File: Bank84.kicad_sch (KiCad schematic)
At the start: 1 part, among them U1 XCKU5P-FFVB676

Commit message: finishing schematic
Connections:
- net IO_L11N_AD1N_84_N: now reaches U1.AA13 (IO_L11N_AD1N_84_N)
- net IO_L8P_HDGC_AD4P_84_P: now reaches U1.AA14 (IO_L8P_HDGC_AD4P_84_P)
- net IO_L7N_HDGC_AD5N_84_N: now reaches U1.AA15 (IO_L7N_HDGC_AD5N_84_N)
- net IO_L8N_HDGC_AD4N_84_N: now reaches U1.AB14 (IO_L8N_HDGC_AD4N_84_N)
- net IO_L6P_HDGC_AD6P_84_P: now reaches U1.AB15 (IO_L6P_HDGC_AD6P_84_P)
- net IO_L6N_HDGC_AD6N_84_N: now reaches U1.AB16 (IO_L6N_HDGC_AD6N_84_N)
- net IO_L5P_HDGC_AD7P_84_P: now reaches U1.AC13 (IO_L5P_HDGC_AD7P_84_P)
- net IO_L5N_HDGC_AD7N_84_N: now reaches U1.AC14 (IO_L5N_HDGC_AD7N_84_N)
- net IO_L4P_AD8P_84_P: now reaches U1.AD13 (IO_L4P_AD8P_84_P)
- net IO_L4N_AD8N_84_N: now reaches U1.AD14 (IO_L4N_AD8N_84_N)
- net IO_L3P_AD9P_84_P: now reaches U1.AD15 (IO_L3P_AD9P_84_P)
- net IO_L2P_AD10P_84_P: now reaches U1.AE13 (IO_L2P_AD10P_84_P)
- net IO_L3N_AD9N_84_N: now reaches U1.AE15 (IO_L3N_AD9N_84_N)
- net IO_L2N_AD10N_84_N: now reaches U1.AF13 (IO_L2N_AD10N_84_N)
- net IO_L1P_AD11P_84_P: now reaches U1.AF14 (IO_L1P_AD11P_84_P)
- net IO_L1N_AD11N_84_N: now reaches U1.AF15 (IO_L1N_AD11N_84_N)
- net IO_L12P_AD0P_84_P: now reaches U1.W12 (IO_L12P_AD0P_84_P)
- net IO_L12N_AD0N_84_N: now reaches U1.W13 (IO_L12N_AD0N_84_N)
- net IO_L10P_AD2P_84_P: now reaches U1.W14 (IO_L10P_AD2P_84_P)
- net IO_L10N_AD2N_84_N: now reaches U1.W15 (IO_L10N_AD2N_84_N)
- net IO_L9P_AD3P_84_P: now reaches U1.W16 (IO_L9P_AD3P_84_P)
- net IO_L11P_AD1P_84_P: now reaches U1.Y13 (IO_L11P_AD1P_84_P)
- net IO_L7P_HDGC_AD5P_84_P: now reaches U1.Y15 (IO_L7P_HDGC_AD5P_84_P)
- net IO_L9N_AD3N_84_N: now reaches U1.Y16 (IO_L9N_AD3N_84_N)
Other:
- moved on the sheet: U1G

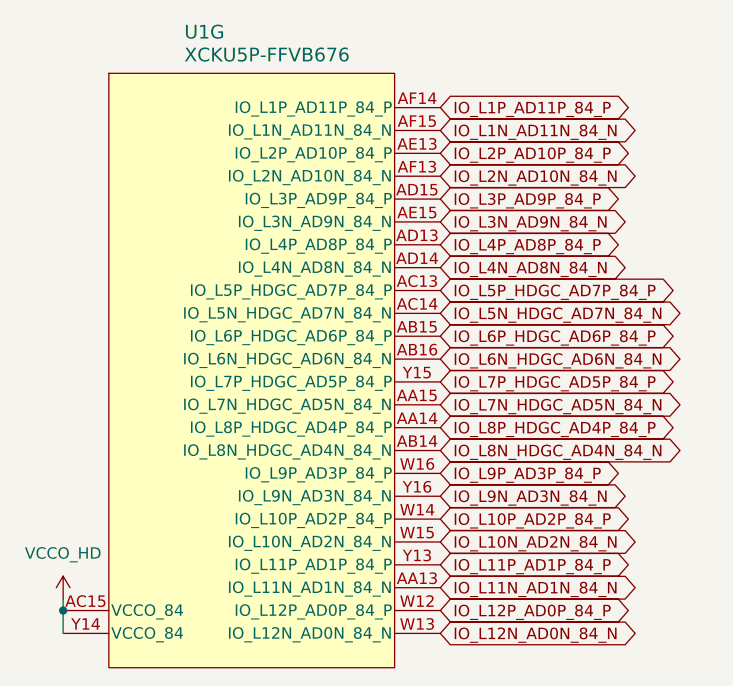
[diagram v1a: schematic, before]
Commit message: change net name to of IO diff pairs, add a scripts for name modification
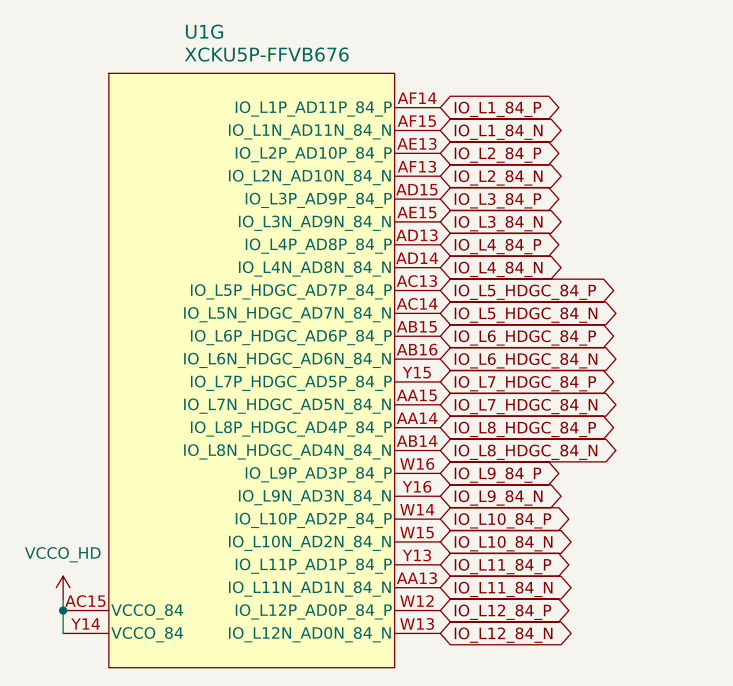
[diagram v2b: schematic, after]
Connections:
- net IO_L10N_AD2N_84_N renamed IO_L10_84_N
- net IO_L10P_AD2P_84_P renamed IO_L10_84_P
- net IO_L11N_AD1N_84_N renamed IO_L11_84_N
- net IO_L11P_AD1P_84_P renamed IO_L11_84_P
- net IO_L12N_AD0N_84_N renamed IO_L12_84_N
- net IO_L12P_AD0P_84_P renamed IO_L12_84_P
- net IO_L1N_AD11N_84_N renamed IO_L1_84_N
- net IO_L1P_AD11P_84_P renamed IO_L1_84_P
- net IO_L2N_AD10N_84_N renamed IO_L2_84_N
- net IO_L2P_AD10P_84_P renamed IO_L2_84_P
- net IO_L3N_AD9N_84_N renamed IO_L3_84_N
- net IO_L3P_AD9P_84_P renamed IO_L3_84_P
- net IO_L4N_AD8N_84_N renamed IO_L4_84_N
- net IO_L4P_AD8P_84_P renamed IO_L4_84_P
- net IO_L5N_HDGC_AD7N_84_N renamed IO_L5_HDGC_84_N
- net IO_L5P_HDGC_AD7P_84_P renamed IO_L5_HDGC_84_P
- net IO_L6N_HDGC_AD6N_84_N renamed IO_L6_HDGC_84_N
- net IO_L6P_HDGC_AD6P_84_P renamed IO_L6_HDGC_84_P
- net IO_L7N_HDGC_AD5N_84_N renamed IO_L7_HDGC_84_N
- net IO_L7P_HDGC_AD5P_84_P renamed IO_L7_HDGC_84_P
- net IO_L8N_HDGC_AD4N_84_N renamed IO_L8_HDGC_84_N
- net IO_L8P_HDGC_AD4P_84_P renamed IO_L8_HDGC_84_P
- net IO_L9N_AD3N_84_N renamed IO_L9_84_N
- net IO_L9P_AD3P_84_P renamed IO_L9_84_P
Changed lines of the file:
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@@
 		)
 	)
-	(global_label "IO_L6N_HDGC_AD6N_84_N"
+	(global_label "IO_L6_HDGC_84_N"
 		(shape bidirectional)
 		(at 92.71 78.74 0)
@@
 		)
 	)
-	(global_label "IO_L12P_AD0P_84_P"
+	(global_label "IO_L12_84_P"
 		(shape bidirectional)
 		(at 92.71 106.68 0)
@@
 		)
 	)
-	(global_label "IO_L11P_AD1P_84_P"
+	(global_label "IO_L11_84_P"
 		(shape bidirectional)
 		(at 92.71 101.6 0)
@@
 		)
 	)
-	(global_label "IO_L3P_AD9P_84_P"
+	(global_label "IO_L3_84_P"
 		(shape bidirectional)
 		(at 92.71 60.96 0)
@@
 		)
 	)
-	(global_label "IO_L7N_HDGC_AD5N_84_N"
+	(global_label "IO_L7_HDGC_84_N"
 		(shape bidirectional)
 		(at 92.71 83.82 0)
@@
 		)
 	)
-	(global_label "IO_L5N_HDGC_AD7N_84_N"
+	(global_label "IO_L5_HDGC_84_N"
 		(shape bidirectional)
 		(at 92.71 73.66 0)
@@
 		)
 	)
-	(global_label "IO_L10P_AD2P_84_P"
+	(global_label "IO_L10_84_P"
 		(shape bidirectional)
 		(at 92.71 96.52 0)
@@
 		)
 	)
-	(global_label "IO_L9P_AD3P_84_P"
+	(global_label "IO_L9_84_P"
 		(shape bidirectional)
 		(at 92.71 91.44 0)
@@
 		)
 	)
-	(global_label "IO_L4N_AD8N_84_N"
+	(global_label "IO_L4_84_N"
 		(shape bidirectional)
 		(at 92.71 68.58 0)
@@
 		)
 	)
-	(global_label "IO_L10N_AD2N_84_N"
+	(global_label "IO_L10_84_N"
 		(shape bidirectional)
 		(at 92.71 99.06 0)
@@
 		)
 	)
-	(global_label "IO_L1P_AD11P_84_P"
+	(global_label "IO_L1_84_P"
 		(shape bidirectional)
 		(at 92.71 50.8 0)
@@
 		)
 	)
-	(global_label "IO_L11N_AD1N_84_N"
+	(global_label "IO_L11_84_N"
 		(shape bidirectional)
 		(at 92.71 104.14 0)
@@
 		)
 	)
-	(global_label "IO_L12N_AD0N_84_N"
+	(global_label "IO_L12_84_N"
 		(shape bidirectional)
 		(at 92.71 109.22 0)
@@
 		)
 	)
-	(global_label "IO_L8P_HDGC_AD4P_84_P"
+	(global_label "IO_L8_HDGC_84_P"
 		(shape bidirectional)
 		(at 92.71 86.36 0)
@@
 		)
 	)
-	(global_label "IO_L2N_AD10N_84_N"
+	(global_label "IO_L2_84_N"
 		(shape bidirectional)
 		(at 92.71 58.42 0)
@@
 		)
 	)
-	(global_label "IO_L2P_AD10P_84_P"
+	(global_label "IO_L2_84_P"
 		(shape bidirectional)
 		(at 92.71 55.88 0)
@@
 		)
 	)
-	(global_label "IO_L3N_AD9N_84_N"
+	(global_label "IO_L3_84_N"
 		(shape bidirectional)
 		(at 92.71 63.5 0)
@@
 		)
 	)
-	(global_label "IO_L1N_AD11N_84_N"
+	(global_label "IO_L1_84_N"
 		(shape bidirectional)
 		(at 92.71 53.34 0)
@@
 		)
 	)
-	(global_label "IO_L5P_HDGC_AD7P_84_P"
+	(global_label "IO_L5_HDGC_84_P"
 		(shape bidirectional)
 		(at 92.71 71.12 0)
@@
 		)
 	)
-	(global_label "IO_L8N_HDGC_AD4N_84_N"
+	(global_label "IO_L8_HDGC_84_N"
 		(shape bidirectional)
 		(at 92.71 88.9 0)
@@
 		)
 	)
-	(global_label "IO_L9N_AD3N_84_N"
+	(global_label "IO_L9_84_N"
 		(shape bidirectional)
 		(at 92.71 93.98 0)
@@
 		)
 	)
-	(global_label "IO_L6P_HDGC_AD6P_84_P"
+	(global_label "IO_L6_HDGC_84_P"
 		(shape bidirectional)
 		(at 92.71 76.2 0)
@@
 		)
 	)
-	(global_label "IO_L7P_HDGC_AD5P_84_P"
+	(global_label "IO_L7_HDGC_84_P"
 		(shape bidirectional)
 		(at 92.71 81.28 0)
@@
 		)
 	)
-	(global_label "IO_L4P_AD8P_84_P"
+	(global_label "IO_L4_84_P"
 		(shape bidirectional)
 		(at 92.71 66.04 0)
